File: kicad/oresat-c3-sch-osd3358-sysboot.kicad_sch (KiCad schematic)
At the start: 27 parts, among them J6 Conn_01x03, U1 OSD3358-512M-BSM

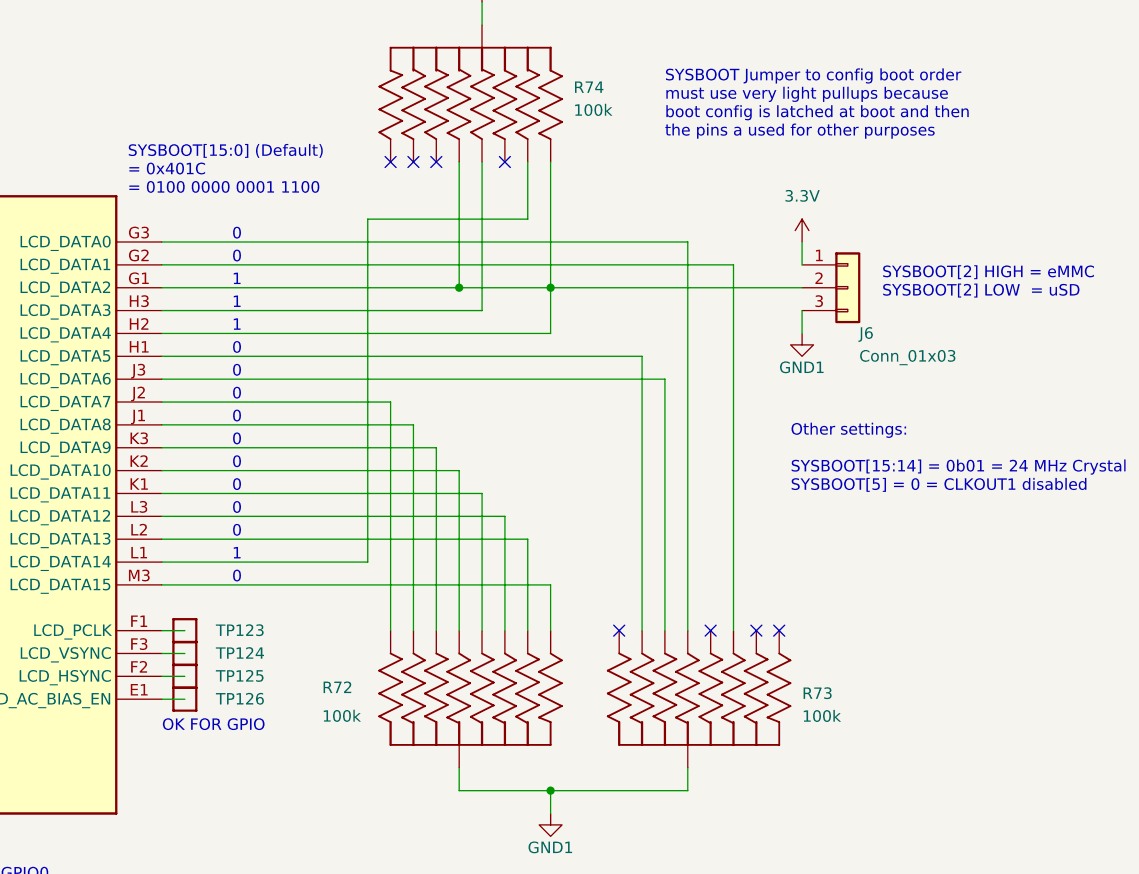
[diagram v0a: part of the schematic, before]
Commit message: routed everything but some minor lines and the radios. About to move the octavo and EVERYTHING else, wish me luck. Should give enough room for the radios!
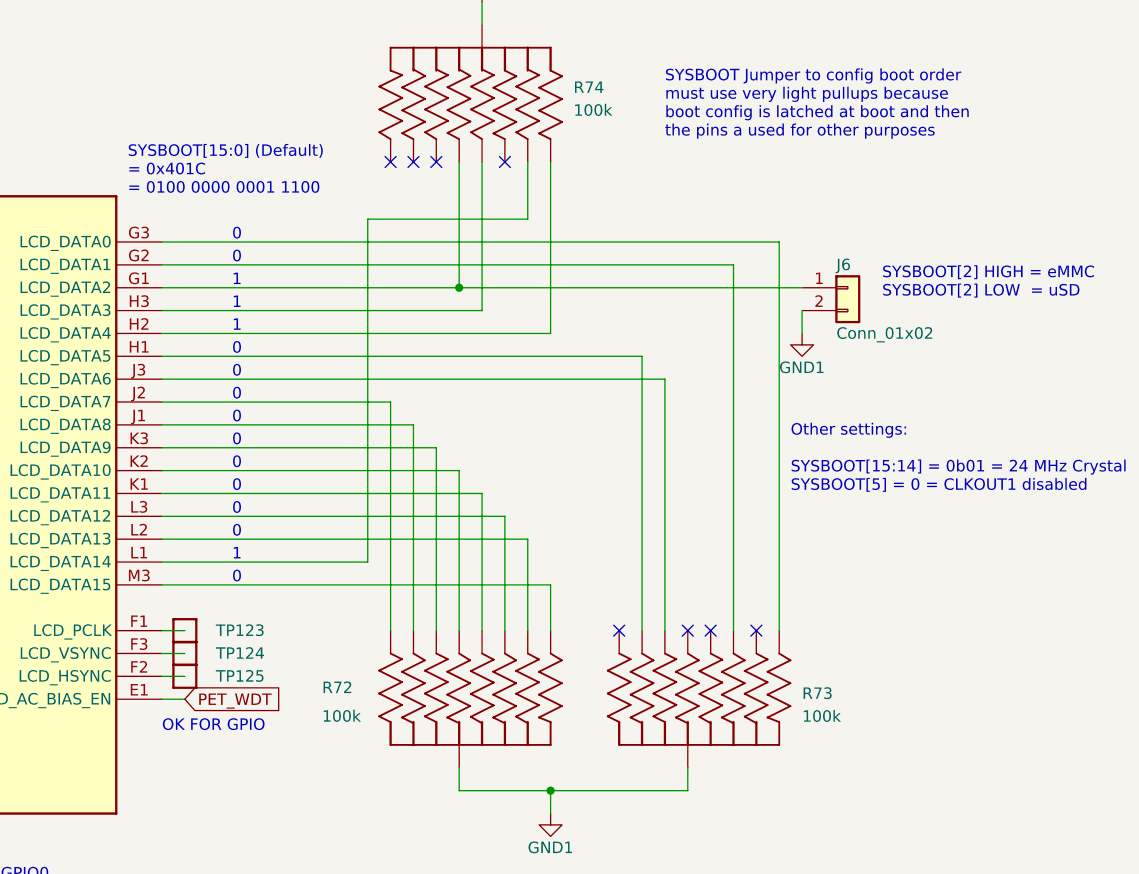
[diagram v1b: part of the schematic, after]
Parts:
- removed J6: Conn_01x03, Connector_PinHeader_2.54mm:PinHeader_1x03_P2.54mm_Vertical, symbol Connector_Generic:Conn_01x03
- removed TP126: Test-Point, oresat-misc:TestPoint_Pad_D1.0mm, symbol oresat-misc:Test-Point-1mm-round
- added J6: Conn_01x02, Connector_PinHeader_2.54mm:PinHeader_1x02_P2.54mm_Vertical, symbol Connector_Generic:Conn_01x02
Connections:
- net GND1: now also J6.2 (Pin_2)
- net at R73.1 (11): now also U1.G3 (LCD_DATA0)
- net at R73.3 (33): no longer U1.G3 (LCD_DATA0)
- net at R74.8 (88), U1.G1 (LCD_DATA2): now also J6.1 (Pin_1); no longer R74.6 (66), U1.H2 (LCD_DATA4)
- net PET_WDT: now reaches U1.E1 (LCD_AC_BIAS_EN)
- new net: R74.6 (66), U1.H2 (LCD_DATA4)
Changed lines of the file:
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@@
     (rev "6.0")
-  )
-  (junction (at 220.98 134.62) (diameter 0) (color 0 0 0 0)
   )
   (junction (at 220.98 190.5) (diameter 0) (color 0 0 0 0)
@@
   (no_connect (at 208.28 120.65))
   (no_connect (at 205.74 120.65))
-  (no_connect (at 246.38 172.72))
+  (no_connect (at 228.6 172.72))
   (no_connect (at 203.2 120.65))
   (no_connect (at 215.9 120.65))
   (no_connect (at 238.76 172.72))
-  (no_connect (at 228.6 172.72))
+  (no_connect (at 236.22 172.72))
   (no_connect (at 243.84 172.72))
   (wire (pts (xy 218.44 120.65) (xy 218.44 127))
@@
     (stroke (width 0) (type default))
   )
-  (wire (pts (xy 220.98 134.62) (xy 248.92 134.62))
+  (wire (pts (xy 210.82 134.62) (xy 248.92 134.62))
     (stroke (width 0) (type default))
   )
@@
     (stroke (width 0) (type default))
   )
-  (wire (pts (xy 177.8 129.54) (xy 236.22 129.54))
+  (wire (pts (xy 177.8 129.54) (xy 246.38 129.54))
     (stroke (width 0) (type default))
   )
@@
     (stroke (width 0) (type default))
   )
-  (wire (pts (xy 248.92 129.54) (xy 248.92 132.08))
-    (stroke (width 0) (type default))
-  )
   (wire (pts (xy 177.8 132.08) (xy 241.3 132.08))
     (stroke (width 0) (type default))
@@
     (stroke (width 0) (type default))
   )
-  (wire (pts (xy 236.22 129.54) (xy 236.22 172.72))
-    (stroke (width 0) (type default))
-  )
   (wire (pts (xy 248.92 137.16) (xy 248.92 139.7))
     (stroke (width 0) (type default))
@@
     (stroke (width 0) (type default))
   )
-  (wire (pts (xy 220.98 134.62) (xy 210.82 134.62))
-    (stroke (width 0) (type default))
-  )
   (polyline (pts (xy 133.35 237.49) (xy 161.29 237.49))
     (stroke (width 0) (type default))
@@
     (stroke (width 0) (type default))
   )
-  (wire (pts (xy 220.98 134.62) (xy 220.98 139.7))
-    (stroke (width 0) (type default))
-  )
   (wire (pts (xy 177.8 162.56) (xy 218.44 162.56))
     (stroke (width 0) (type default))
@@
     (stroke (width 0) (type default))
   )
-  (wire (pts (xy 220.98 120.65) (xy 220.98 134.62))
+  (wire (pts (xy 246.38 129.54) (xy 246.38 172.72))
+    (stroke (width 0) (type default))
+  )
+  (wire (pts (xy 220.98 120.65) (xy 220.98 139.7))
     (stroke (width 0) (type default))
   )
@@
   (text "0" (at 186.69 129.54 0)
     (effects (font (size 1.27 1.27)) (justify right bottom))
+  )
+  (global_label "PET_WDT" (shape input) (at 180.34 180.34 0) (fields_autoplaced)
+    (effects (font (size 1.27 1.27)) (justify left))
+    (property "Intersheetrefs" "${INTERSHEET_REFS}" (at 191.289 180.34 0)
+      (effects (font (size 1.27 1.27)) (justify left))
+    )
   )
   (symbol (lib_id "oresat-misc:Test-Point-1mm-round") (at 114.3 162.56 270) (unit 1)
@@
         (path "/65d12cdd-c326-4033-9053-c59fa4e0b25e/0c732c1e-ab0d-41ac-9d77-9d7763333b6f"
           (reference "TP123") (unit 1)
-        )
-      )
-    )
-  )
-  (symbol (lib_id "Connector_Generic:Conn_01x03") (at 254 134.62 0) (unit 1)
-    (in_bom yes) (on_board yes) (dnp no)
-    (property "Reference" "J6" (at 255.27 139.7 0)
-      (effects (font (size 1.27 1.27)) (justify left))
-    )
-    (property "Value" "Conn_01x03" (at 255.27 142.24 0)
-      (effects (font (size 1.27 1.27)) (justify left))
-    )
-    (property "Footprint" "Connector_PinHeader_2.54mm:PinHeader_1x03_P2.54mm_Vertical" (at 254 134.62 0)
-      (effects (font (size 1.27 1.27)) hide)
-    )
-    (property "Datasheet" "~" (at 254 134.62 0)
-      (effects (font (size 1.27 1.27)) hide)
-    )
-    (pin "1")
-    (pin "2")
-    (pin "3")
-    (instances
-      (project "oresat-c3"
-        (path "/65d12cdd-c326-4033-9053-c59fa4e0b25e/0c732c1e-ab0d-41ac-9d77-9d7763333b6f"
-          (reference "J6") (unit 1)
-        )
-      )
-    )
-  )
-  (symbol (lib_id "oresat-power:3.3V") (at 248.92 129.54 0) (unit 1)
-    (in_bom yes) (on_board yes) (dnp no) (fields_autoplaced)
-    (property "Reference" "#3V0109" (at 248.92 133.35 0)
-      (effects (font (size 1.27 1.27)) hide)
-    )
-    (property "Value" "3.3V" (at 248.92 124.46 0)
-      (effects (font (size 1.27 1.27)))
-    )
-    (property "Footprint" "" (at 248.92 129.54 0)
-      (effects (font (size 1.27 1.27)) hide)
-    )
-    (property "Datasheet" "" (at 248.92 129.54 0)
-      (effects (font (size 1.27 1.27)) hide)
-    )
-    (pin "1")
-    (instances
-      (project "oresat-c3"
-        (path "/65d12cdd-c326-4033-9053-c59fa4e0b25e/0c732c1e-ab0d-41ac-9d77-9d7763333b6f"
-          (reference "#3V0109") (unit 1)
         )
       )
@@
     )
   )
+  (symbol (lib_id "Connector_Generic:Conn_01x02") (at 254 134.62 0) (unit 1)
+    (in_bom yes) (on_board yes) (dnp no)
+    (property "Reference" "J6" (at 252.73 132.08 0)
+      (effects (font (size 1.27 1.27)) (justify left))
+    )
+    (property "Value" "Conn_01x02" (at 252.73 139.7 0)
+      (effects (font (size 1.27 1.27)) (justify left))
+    )
+    (property "Footprint" "Connector_PinHeader_2.54mm:PinHeader_1x02_P2.54mm_Vertical" (at 254 134.62 0)
+      (effects (font (size 1.27 1.27)) hide)
+    )
+    (property "Datasheet" "~" (at 254 134.62 0)
+      (effects (font (size 1.27 1.27)) hide)
+    )
+    (pin "1")
+    (pin "2")
+    (instances
+      (project "oresat-c3"
+        (path "/65d12cdd-c326-4033-9053-c59fa4e0b25e/0c732c1e-ab0d-41ac-9d77-9d7763333b6f"
+          (reference "J6") (unit 1)
+        )
+      )
+    )
+  )
   (symbol (lib_id "oresat-misc:Test-Point-1mm-round") (at 114.3 132.08 270) (unit 1)
     (in_bom yes) (on_board yes) (dnp no)
@@
         )
       )
-    )
-  )
-  (symbol (lib_id "oresat-misc:Test-Point-1mm-round") (at 180.34 180.34 90) (unit 1)
-    (in_bom yes) (on_board yes) (dnp no)
-    (property "Reference" "TP126" (at 189.23 180.34 90)
-      (effects (font (size 1.27 1.27)) (justify left))
-    )
-    (property "Value" "Test-Point" (at 177.8 180.34 0)
-      (effects (font (size 1.27 1.27)) hide)
-    )
-    (property "Footprint" "oresat-misc:TestPoint_Pad_D1.0mm" (at 170.18 180.34 0)
-      (effects (font (size 1.27 1.27)) hide)
-    )
-    (property "Datasheet" "" (at 180.34 180.34 0)
-      (effects (font (size 1.27 1.27)) hide)
-    )
-    (pin "1")
-    (instances
-      (project "oresat-c3"
-        (path "/65d12cdd-c326-4033-9053-c59fa4e0b25e/0c732c1e-ab0d-41ac-9d77-9d7763333b6f"
-          (reference "TP126") (unit 1)
-        )
-      )

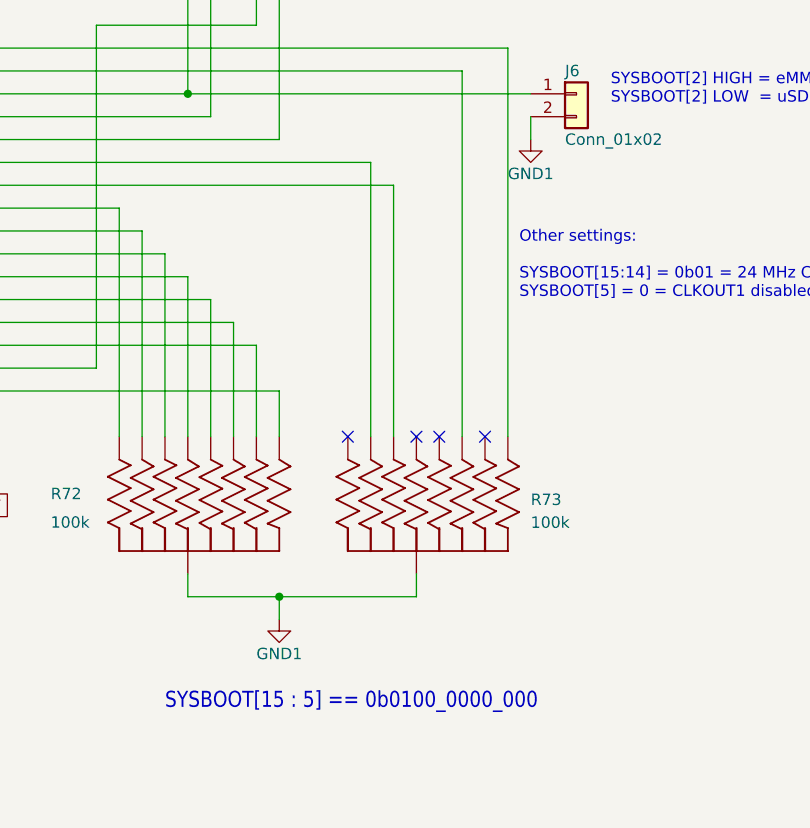
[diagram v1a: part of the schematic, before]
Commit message: Switched all grounds to a single ground, because I can't find a way to overlap ground planes in KiCAD. That's actually not terrible, however, because KiCAD has an anti-plane feature which I used to cut the ground plane between UHF and L radios and L radio and Octavo. So actually I think it came out better than having separate ground planes. Only thing left now are the ~ 40 connections to the Octavo.
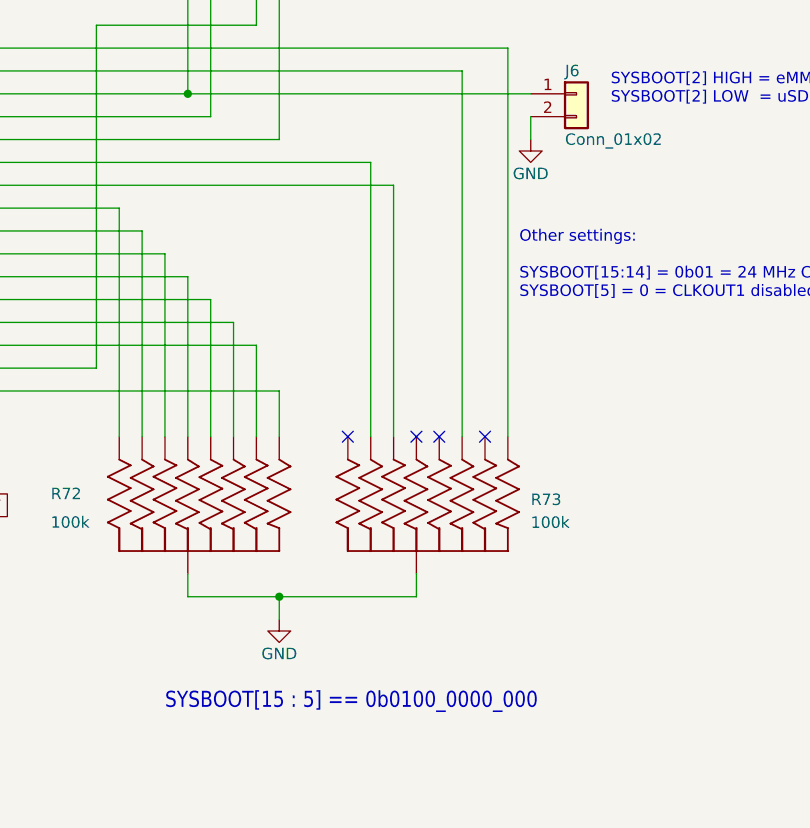
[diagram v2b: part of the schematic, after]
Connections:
- net GND1 renamed GND
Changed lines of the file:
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@@
     )
   )
-  (symbol (lib_id "power:GND1") (at 220.98 193.04 0) (unit 1)
-    (in_bom yes) (on_board yes) (dnp no)
-    (property "Reference" "#PWR0159" (at 220.98 199.39 0)
-      (effects (font (size 1.27 1.27)) hide)
-    )
-    (property "Value" "GND1" (at 220.98 196.85 0)
+  (symbol (lib_id "power:GND") (at 220.98 193.04 0) (unit 1)
+    (in_bom yes) (on_board yes) (dnp no)
+    (property "Reference" "#PWR?" (at 220.98 199.39 0)
+      (effects (font (size 1.27 1.27)) hide)
+    )
+    (property "Value" "GND" (at 220.98 196.85 0)
       (effects (font (size 1.27 1.27)))
     )
@@
       (project "oresat-c3"
         (path "/65d12cdd-c326-4033-9053-c59fa4e0b25e/0c732c1e-ab0d-41ac-9d77-9d7763333b6f"
-          (reference "#PWR0159") (unit 1)
+          (reference "#PWR?") (unit 1)
         )
       )
@@
     )
   )
-  (symbol (lib_id "power:GND1") (at 248.92 139.7 0) (unit 1)
-    (in_bom yes) (on_board yes) (dnp no)
-    (property "Reference" "#PWR0158" (at 248.92 146.05 0)
-      (effects (font (size 1.27 1.27)) hide)
-    )
-    (property "Value" "GND1" (at 248.92 143.51 0)
+  (symbol (lib_id "power:GND") (at 248.92 139.7 0) (unit 1)
+    (in_bom yes) (on_board yes) (dnp no)
+    (property "Reference" "#PWR?" (at 248.92 146.05 0)
+      (effects (font (size 1.27 1.27)) hide)
+    )
+    (property "Value" "GND" (at 248.92 143.51 0)
       (effects (font (size 1.27 1.27)))
     )
@@
       (project "oresat-c3"
         (path "/65d12cdd-c326-4033-9053-c59fa4e0b25e/0c732c1e-ab0d-41ac-9d77-9d7763333b6f"
-          (reference "#PWR0158") (unit 1)
-        )
-      )
+          (reference "#PWR?") (unit 1)
+        )
+      )
